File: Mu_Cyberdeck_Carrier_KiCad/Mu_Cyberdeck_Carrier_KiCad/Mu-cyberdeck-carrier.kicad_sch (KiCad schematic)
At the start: 6 parts

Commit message: Added BQ25798 Power IC
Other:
- sheet Gigabit Ethernet renamed Gigabit Ethernet - UNUSED?
- sheet LattePanda Module1 renamed LattePanda Module
- sheet PCIe x4 renamed PCIe x4 - UNUSED
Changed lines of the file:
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@@
 			(project "Mu-cyberdeck-carrier"
 				(path "/2a6d114a-7fd7-4207-b5f7-4ea9c34f36aa"
-					(page "11")
+					(page "2")
 				)
 			)
@@
 			(color 0 0 0 0)
 		)
-		(property "Sheetname" "PCIe x4"
+		(property "Sheetname" "PCIe x4 - UNUSED"
 			(at 29.21 154.2284 0)
 			(show_name no)
@@
 			(project "Mu-cyberdeck-carrier"
 				(path "/2a6d114a-7fd7-4207-b5f7-4ea9c34f36aa"
-					(page "3")
+					(page "10")
 				)
 			)
@@
 			(color 0 0 0 0)
 		)
-		(property "Sheetname" "LattePanda Module1"
+		(property "Sheetname" "LattePanda Module"
 			(at 227.33 95.8084 0)
 			(show_name no)
@@
 			(project "Mu-cyberdeck-carrier"
 				(path "/2a6d114a-7fd7-4207-b5f7-4ea9c34f36aa"
-					(page "4")
+					(page "3")
 				)
 			)
@@
 			(project "Mu-cyberdeck-carrier"
 				(path "/2a6d114a-7fd7-4207-b5f7-4ea9c34f36aa"
-					(page "10")
+					(page "6")
 				)
 			)
@@
 			(project "Mu-cyberdeck-carrier"
 				(path "/2a6d114a-7fd7-4207-b5f7-4ea9c34f36aa"
-					(page "9")
+					(page "5")
 				)
 			)
@@
 			(color 0 0 0 0)
 		)
-		(property "Sheetname" "Gigabit Ethernet"
+		(property "Sheetname" "Gigabit Ethernet - UNUSED?"
 			(at 62.23 154.2284 0)
 			(show_name no)
@@
 			(project "Mu-cyberdeck-carrier"
 				(path "/2a6d114a-7fd7-4207-b5f7-4ea9c34f36aa"
-					(page "6")
+					(page "9")
 				)
 			)
@@
 			(project "Mu-cyberdeck-carrier"
 				(path "/2a6d114a-7fd7-4207-b5f7-4ea9c34f36aa"
-					(page "5")
-				)
-			)
+					(page "4")
+				)
+			)

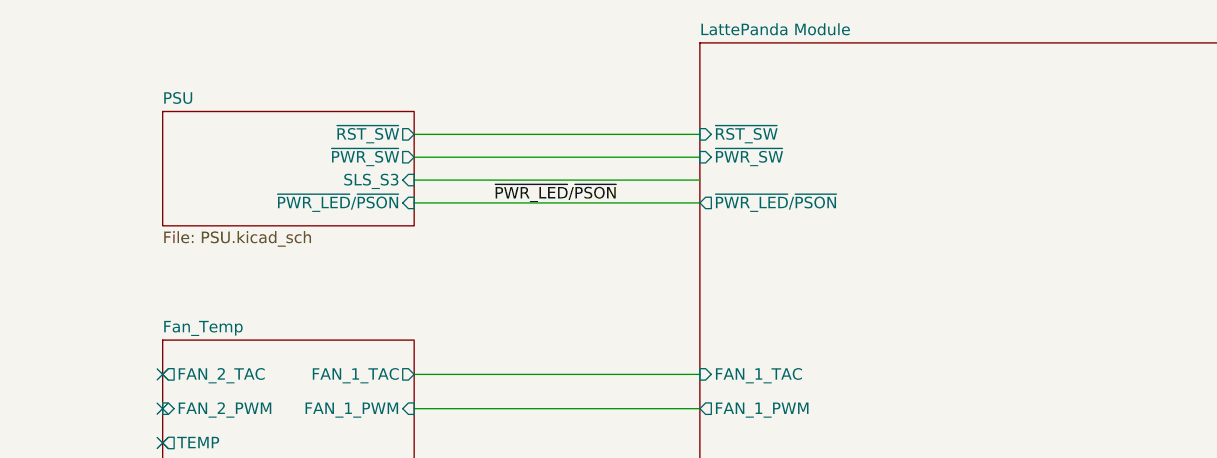
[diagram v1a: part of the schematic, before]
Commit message: Added 'BQ27441DRZT-G1A' fuel guage IC.
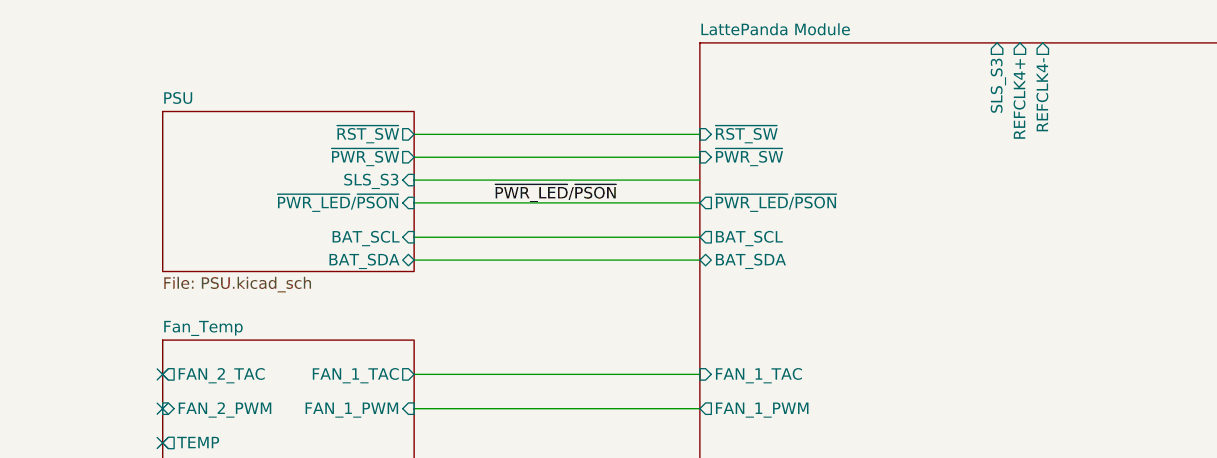
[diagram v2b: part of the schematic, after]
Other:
- sheet LattePanda Module ports: added BAT_SCL, BAT_SDA, REFCLK4+, REFCLK4-, SLS_S3; removed none
- sheet PSU ports: added BAT_SCL, BAT_SDA; removed none
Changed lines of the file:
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@@
+	(wire
+		(pts
+			(xy 195.58 120.65) (xy 227.33 120.65)
+		)
+		(stroke
+			(width 0)
+			(type default)
+		)
+	)
 	(wire
 		(pts
@@
 		(pts
 			(xy 341.63 105.41) (xy 367.03 105.41)
+		)
+		(stroke
+			(width 0)
+			(type default)
+		)
+	)
+	(wire
+		(pts
+			(xy 195.58 118.11) (xy 227.33 118.11)
 		)
 		(stroke
@@
 			)
 		)
+		(pin "BAT_SCL" output
+			(at 227.33 118.11 180)
+			(effects
+				(font
+					(size 1.27 1.27)
+				)
+				(justify left)
+			)
+		)
+		(pin "BAT_SDA" bidirectional
+			(at 227.33 120.65 180)
+			(effects
+				(font
+					(size 1.27 1.27)
+				)
+				(justify left)
+			)
+		)
+		(pin "REFCLK4+" output
+			(at 262.89 96.52 90)
+			(effects
+				(font
+					(size 1.27 1.27)
+				)
+				(justify right)
+			)
+		)
+		(pin "REFCLK4-" output
+			(at 265.43 96.52 90)
+			(effects
+				(font
+					(size 1.27 1.27)
+				)
+				(justify right)
+			)
+		)
+		(pin "SLS_S3" output
+			(at 260.35 96.52 90)
+			(effects
+				(font
+					(size 1.27 1.27)
+				)
+				(justify right)
+			)
+		)
 		(instances
 			(project "Mu-cyberdeck-carrier"
@@
 	(sheet
 		(at 167.64 104.14)
-		(size 27.94 12.7)
+		(size 27.94 17.78)
 		(exclude_from_sim no)
 		(in_bom yes)
@@
 		)
 		(property "Sheetfile" "PSU.kicad_sch"
-			(at 167.64 117.4246 0)
+			(at 167.64 122.5046 0)
 			(show_name no)
 			(do_not_autoplace no)
@@
 			(effects
 				(font
+					(size 1.27 1.27)
+				)
+				(justify right)
+			)
+		)
+		(pin "BAT_SDA" bidirectional
+			(at 195.58 120.65 0)
+			(effects
+				(font
+					(size 1.27 1.27)
+				)
+				(justify right)
+			)
+		)
+		(pin "BAT_SCL" input
+			(at 195.58 118.11 0)
+			(effects
+				(font

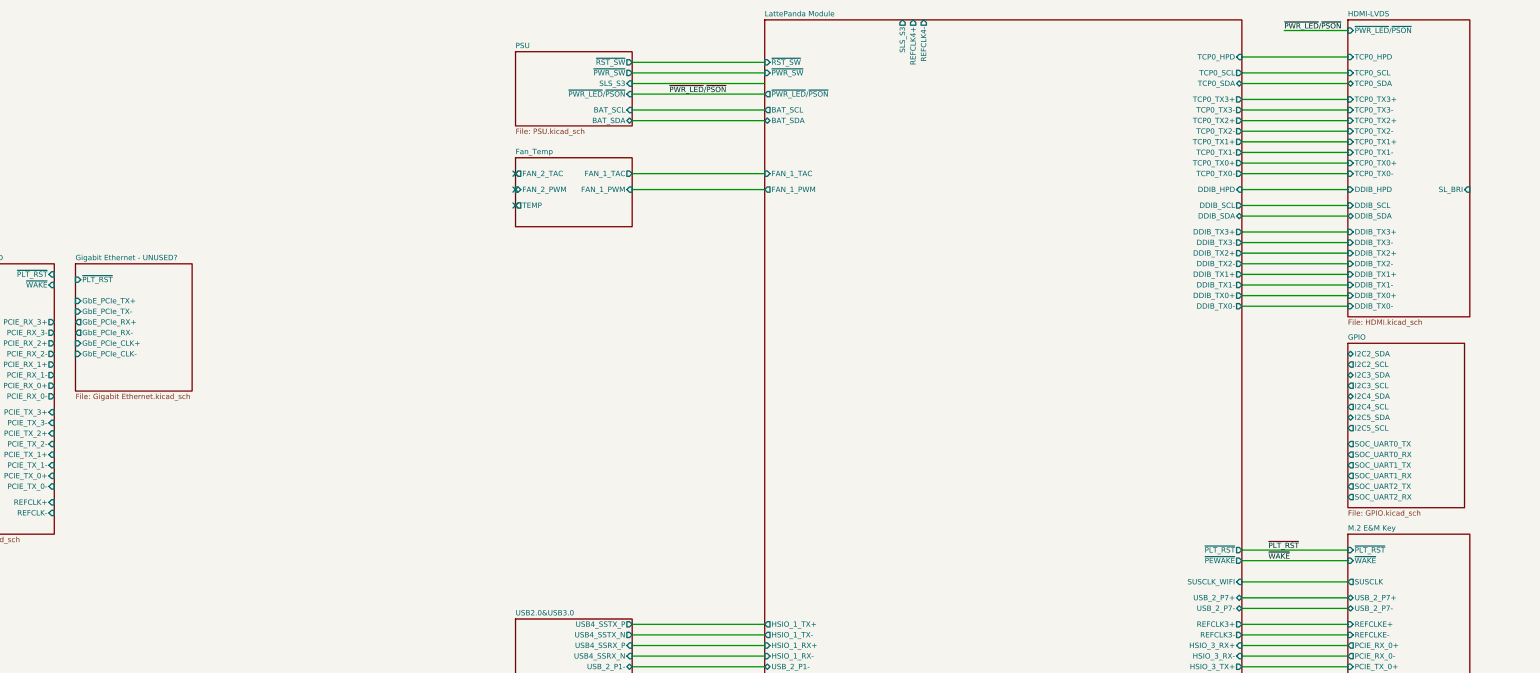
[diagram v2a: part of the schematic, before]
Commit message: CTRL Z, R, PWR Cleanup! Changes Made:
CTRL PWR -> Added Ground Plane and Ground Vias. Moved it out of parent folder CTRL_R upto Root.
CTRL Z ->  Removed Unnecessary ZX pin. Added Ground Plane and Ground Vias.
CTRL R -> Cleaned up pin count, from 14 down to 10. Added Ground Plane and Ground Vias. Made some modifications to the board shape.
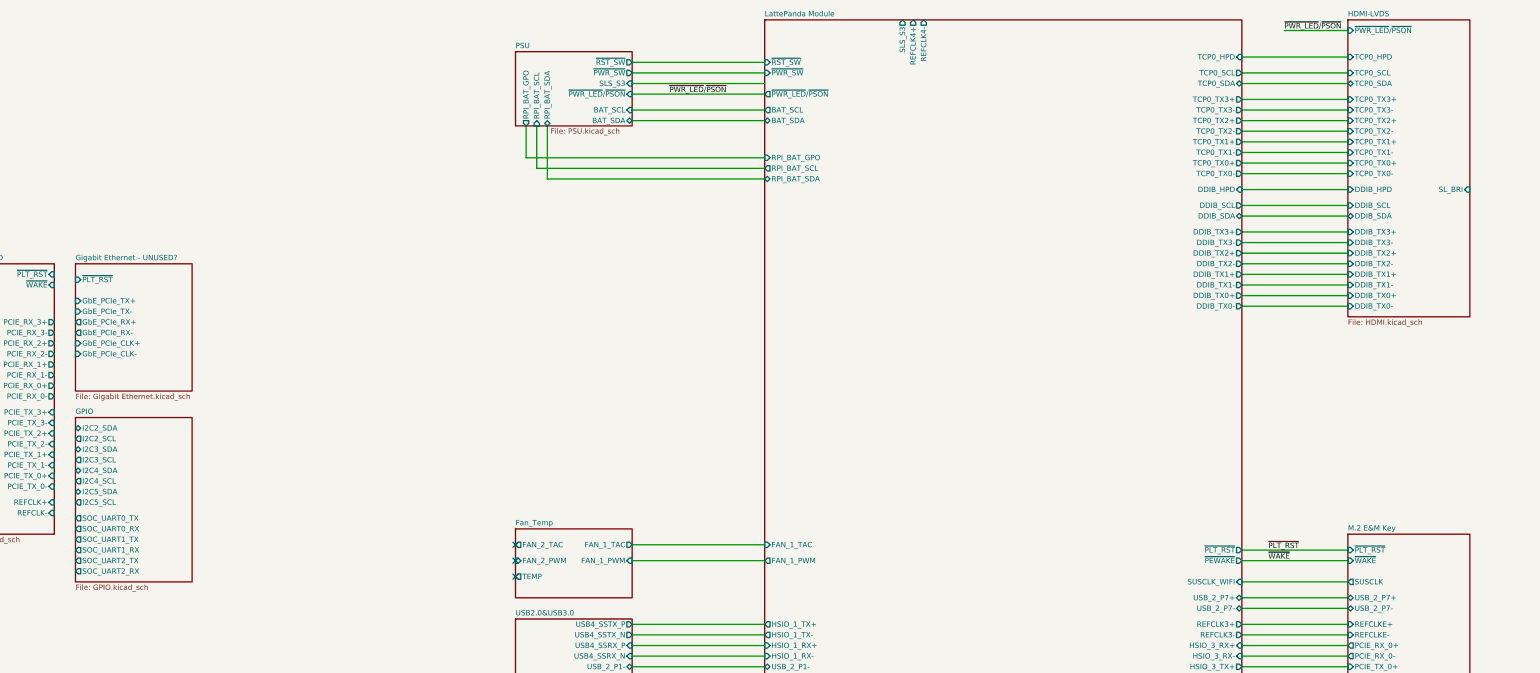
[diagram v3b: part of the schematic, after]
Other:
- sheet LattePanda Module ports: added RPI_BAT_GPO, RPI_BAT_SCL, RPI_BAT_SDA; removed none
- sheet PSU ports: added RPI_BAT_GPO, RPI_BAT_SCL, RPI_BAT_SDA; removed none
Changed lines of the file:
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@@
 	)
 	(no_connect
-		(at 167.64 137.16)
+		(at 167.64 226.06)
 	)
 	(no_connect
-		(at 167.64 140.97)
+		(at 167.64 229.87)
 	)
 	(no_connect
-		(at 167.64 133.35)
+		(at 167.64 222.25)
 	)
 	(wire
@@
 	(wire
 		(pts
+			(xy 175.26 134.62) (xy 175.26 121.92)
+		)
+		(stroke
+			(width 0)
+			(type default)
+		)
+	)
+	(wire
+		(pts
+			(xy 172.72 132.08) (xy 172.72 121.92)
+		)
+		(stroke
+			(width 0)
+			(type default)
+		)
+	)
+	(wire
+		(pts
 			(xy 195.58 274.32) (xy 227.33 274.32)
 		)
@@
 	(wire
 		(pts
+			(xy 170.18 129.54) (xy 227.33 129.54)
+		)
+		(stroke
+			(width 0)
+			(type default)
+		)
+	)
+	(wire
+		(pts
 			(xy 341.63 147.32) (xy 367.03 147.32)
 		)
@@
 	(wire
 		(pts
+			(xy 170.18 121.92) (xy 170.18 129.54)
+		)
+		(stroke
+			(width 0)
+			(type default)
+		)
+	)
+	(wire
+		(pts
 			(xy 195.58 267.97) (xy 227.33 267.97)
 		)
@@
 	(wire
 		(pts
-			(xy 195.58 133.35) (xy 227.33 133.35)
+			(xy 195.58 222.25) (xy 227.33 222.25)
 		)
 		(stroke
@@
 	(wire
 		(pts
+			(xy 227.33 132.08) (xy 172.72 132.08)
+		)
+		(stroke
+			(width 0)
+			(type default)
+		)
+	)
+	(wire
+		(pts
 			(xy 195.58 114.3) (xy 227.33 114.3)
 		)
@@
 	(wire
 		(pts
+			(xy 227.33 134.62) (xy 175.26 134.62)
+		)
+		(stroke
+			(width 0)
+			(type default)
+		)
+	)
+	(wire
+		(pts
 			(xy 195.58 270.51) (xy 227.33 270.51)
 		)
@@
 	(wire
 		(pts
-			(xy 195.58 137.16) (xy 227.33 137.16)
+			(xy 195.58 226.06) (xy 227.33 226.06)
 		)
 		(stroke
@@
 		)
 		(pin "FAN_1_PWM" output
-			(at 227.33 137.16 180)
+			(at 227.33 226.06 180)
 			(effects
 				(font
@@
 		)
 		(pin "FAN_1_TAC" input
-			(at 227.33 133.35 180)
+			(at 227.33 222.25 180)
 			(effects
 				(font
@@
 			)
 		)
+		(pin "RPI_BAT_GPO" input
+			(at 227.33 129.54 180)
+			(effects
+				(font
+					(size 1.27 1.27)
+				)
+				(justify left)
+			)
+		)
+		(pin "RPI_BAT_SCL" output
+			(at 227.33 132.08 180)
+			(effects
+				(font
+					(size 1.27 1.27)
+				)
+				(justify left)
+			)
+		)
+		(pin "RPI_BAT_SDA" bidirectional
+			(at 227.33 134.62 180)
+			(effects
+				(font
+					(size 1.27 1.27)
+				)
+				(justify left)
+			)
+		)
 		(instances
 			(project "Mu-cyberdeck-carrier"
@@
 	)
 	(sheet
-		(at 167.64 129.54)
+		(at 167.64 218.44)
 		(size 27.94 16.51)
 		(exclude_from_sim no)
@@
 		)
 		(property "Sheetname" "Fan_Temp"
-			(at 167.64 128.8284 0)
+			(at 167.64 217.7284 0)
 			(show_name no)
 			(do_not_autoplace no)
@@
 		)
 		(property "Sheetfile" "fan_temp.kicad_sch"
-			(at 167.64 146.6346 0)
+			(at 167.64 235.5346 0)
 			(hide yes)
 			(show_name no)
@@
 		)
 		(pin "FAN_1_TAC" output
-			(at 195.58 133.35 0)
+			(at 195.58 222.25 0)
 			(effects
 				(font
@@
 		)
 		(pin "FAN_1_PWM" input
-			(at 195.58 137.16 0)
+			(at 195.58 226.06 0)
 			(effects
 				(font
@@
 		)
 		(pin "FAN_2_PWM" input
-			(at 167.64 137.16 180)
+			(at 167.64 226.06 180)
 			(effects
 				(font
@@
 		)
 		(pin "FAN_2_TAC" output
-			(at 167.64 133.35 180)
+			(at 167.64 222.25 180)
 			(effects
 				(font
@@
 		)
 		(pin "TEMP" output
-			(at 167.64 140.97 180)
+			(at 167.64 229.87 180)
 			(effects
 				(font
@@
 		(on_board yes)
 		(dnp no)
-		(fields_autoplaced yes)
 		(stroke
 			(width 0.1524)
@@
 		)
 		(property "Sheetfile" "PSU.kicad_sch"
-			(at 167.64 122.5046 0)
+			(at 176.022 122.428 0)
 			(show_name no)
 			(do_not_autoplace no)
@@
 			)
 		)
+		(pin "RPI_BAT_GPO" output
+			(at 170.18 121.92 270)
+			(effects
+				(font
+					(size 1.27 1.27)
+				)
+				(justify left)
+			)
+		)
+		(pin "RPI_BAT_SCL" input
+			(at 172.72 121.92 270)
+			(effects
+				(font
+					(size 1.27 1.27)
+				)
+				(justify left)
+			)
+		)
+		(pin "RPI_BAT_SDA" bidirectional
+			(at 175.26 121.92 270)
+			(effects
+				(font
+					(size 1.27 1.27)
+				)
+				(justify left)
+			)
+		)
 		(instances
 			(project "Mu-cyberdeck-carrier"
@@
 	)
 	(sheet
-		(at 367.03 173.99)
+		(at 62.23 191.77)
 		(size 27.94 39.37)
-		(exclude_from_sim no)
-		(in_bom yes)
+		(exclude_from_sim yes)
+		(in_bom no)
 		(on_board yes)
-		(dnp no)
+		(dnp yes)
 		(fields_autoplaced yes)
 		(stroke
@@
 		)
 		(property "Sheetname" "GPIO"
-			(at 367.03 173.2784 0)
+			(at 62.23 191.0584 0)
 			(show_name no)
 			(do_not_autoplace no)
@@
 		)
 		(property "Sheetfile" "GPIO.kicad_sch"
-			(at 367.03 213.9446 0)
+			(at 62.23 231.7246 0)
 			(show_name no)
 			(do_not_autoplace no)
@@
 		)
 		(pin "I2C2_SCL" output
-			(at 367.03 179.07 180)
+			(at 62.23 196.85 180)
 			(effects
 				(font
@@
 		)
 		(pin "I2C4_SCL" output
-			(at 367.03 189.23 180)
+			(at 62.23 207.01 180)
 			(effects
 				(font
@@
 		)
 		(pin "I2C5_SCL" output
-			(at 367.03 194.31 180)
+			(at 62.23 212.09 180)
 			(effects
 				(font
@@
 		)
 		(pin "I2C3_SCL" output
-			(at 367.03 184.15 180)
+			(at 62.23 201.93 180)
 			(effects
 				(font
@@
 		)
 		(pin "SOC_UART0_TX" output
-			(at 367.03 198.12 180)
+			(at 62.23 215.9 180)
 			(effects
 				(font
@@
 		)
 		(pin "SOC_UART1_TX" output
-			(at 367.03 203.2 180)
+			(at 62.23 220.98 180)
 			(effects
 				(font
@@
 		)
 		(pin "SOC_UART2_TX" output
-			(at 367.03 208.28 180)
+			(at 62.23 226.06 180)
 			(effects
 				(font
@@
 		)
 		(pin "I2C3_SDA" bidirectional
-			(at 367.03 181.61 180)
+			(at 62.23 199.39 180)
 			(effects
 				(font
@@
 		)
 		(pin "I2C4_SDA" bidirectional
-			(at 367.03 186.69 180)
+			(at 62.23 204.47 180)
 			(effects
 				(font
@@
 		)
 		(pin "I2C5_SDA" bidirectional
-			(at 367.03 191.77 180)
+			(at 62.23 209.55 180)
 			(effects
 				(font
@@
 		)
 		(pin "I2C2_SDA" bidirectional
-			(at 367.03 176.53 180)
+			(at 62.23 194.31 180)
 			(effects
 				(font
@@
 		)
 		(pin "SOC_UART0_RX" output
-			(at 367.03 200.66 180)
+			(at 62.23 218.44 180)
 			(effects
 				(font
@@
 		)
 		(pin "SOC_UART2_RX" output
-			(at 367.03 210.82 180)
+			(at 62.23 228.6 180)
 			(effects
 				(font
@@
 		)
 		(pin "SOC_UART1_RX" output
-			(at 367.03 205.74 180)
+			(at 62.23 223.52 180)
 			(effects
 				(font
